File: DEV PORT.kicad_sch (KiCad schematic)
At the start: 11 parts

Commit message: added more notes and documentation
todo:
    - timing analysis to make sure everything fits in 250nS + hold time/prep time
    - logic analysis to ensure correct functionality (am gonna make dumb mistakes!)
    - board layout
    - physical testing!
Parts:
- added D?: (no value), symbol Diode:BAT48JFILM
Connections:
- net +5V: now also U?.48 (VIN), D?.1 (K)
- net at U?.49 (VUSB): now also D?.2 (A)
- no-connect marks 14 -> 13
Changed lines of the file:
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@@
   (no_connect (at 38.1 88.9))
   (no_connect (at 38.1 91.44))
-  (no_connect (at 93.98 21.59))
   (no_connect (at 69.85 113.03))
   (no_connect (at 73.66 113.03))
@@
     (pin "1")
   )
+  (symbol (lib_id "Diode:BAT48JFILM") (at 97.79 21.59 180) (unit 1)
+    (in_bom yes) (on_board yes) (fields_autoplaced)
+    (property "Reference" "D?" (id 0) (at 98.1075 15.24 0))
+    (property "Value" "" (id 1) (at 98.1075 17.78 0))
+    (property "Footprint" "" (id 2) (at 97.79 17.145 0)
+      (effects (font (size 1.27 1.27)) hide)
+    )
+    (property "Datasheet" "www.st.com/resource/en/datasheet/bat48.pdf" (id 3) (at 97.79 21.59 0)
+      (effects (font (size 1.27 1.27)) hide)
+    )
+    (pin "1")
+    (pin "2")
+  )
   (symbol (lib_id "power:+3V3") (at 153.67 81.28 0) (unit 1)
     (in_bom yes) (on_board yes) (fields_autoplaced)
@@
     )
     (property "Datasheet" "" (id 3) (at 251.46 110.49 0)
+      (effects (font (size 1.27 1.27)) hide)
+    )
+    (pin "1")
+  )
+  (symbol (lib_id "power:+5V") (at 93.98 25.4 270) (unit 1)
+    (in_bom yes) (on_board yes) (fields_autoplaced)
+    (property "Reference" "#PWR?" (id 0) (at 90.17 25.4 0)
+      (effects (font (size 1.27 1.27)) hide)
+    )
+    (property "Value" "" (id 1) (at 97.79 25.3999 90)
+      (effects (font (size 1.27 1.27)) (justify left))
+    )
+    (property "Footprint" "" (id 2) (at 93.98 25.4 0)
+      (effects (font (size 1.27 1.27)) hide)
+    )
+    (property "Datasheet" "" (id 3) (at 93.98 25.4 0)
       (effects (font (size 1.27 1.27)) hide)
     )
@@
     (pin "9")
   )
+  (symbol (lib_id "power:+5V") (at 101.6 21.59 270) (unit 1)
+    (in_bom yes) (on_board yes) (fields_autoplaced)
+    (property "Reference" "#PWR?" (id 0) (at 97.79 21.59 0)
+      (effects (font (size 1.27 1.27)) hide)
+    )
+    (property "Value" "" (id 1) (at 105.41 21.5899 90)
+      (effects (font (size 1.27 1.27)) (justify left))
+    )
+    (property "Footprint" "" (id 2) (at 101.6 21.59 0)
+      (effects (font (size 1.27 1.27)) hide)
+    )
+    (property "Datasheet" "" (id 3) (at 101.6 21.59 0)
+      (effects (font (size 1.27 1.27)) hide)
+    )
+    (pin "1")
+  )
   (symbol (lib_id "power:+3V3") (at 215.9 128.27 0) (unit 1)

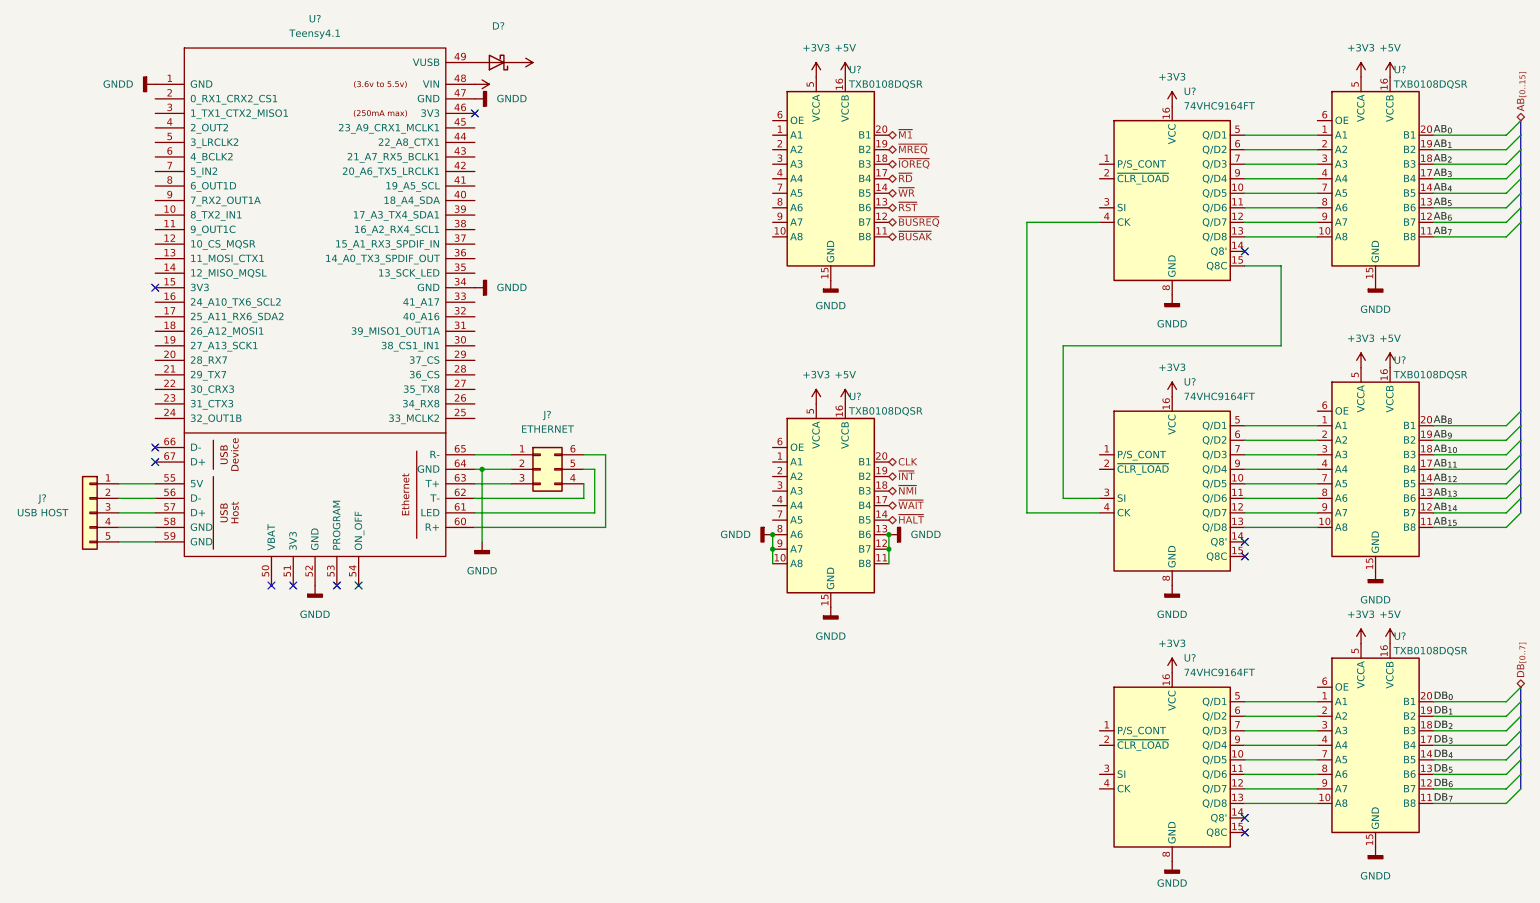
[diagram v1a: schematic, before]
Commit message: some clean up and simplification, as well as some renaming
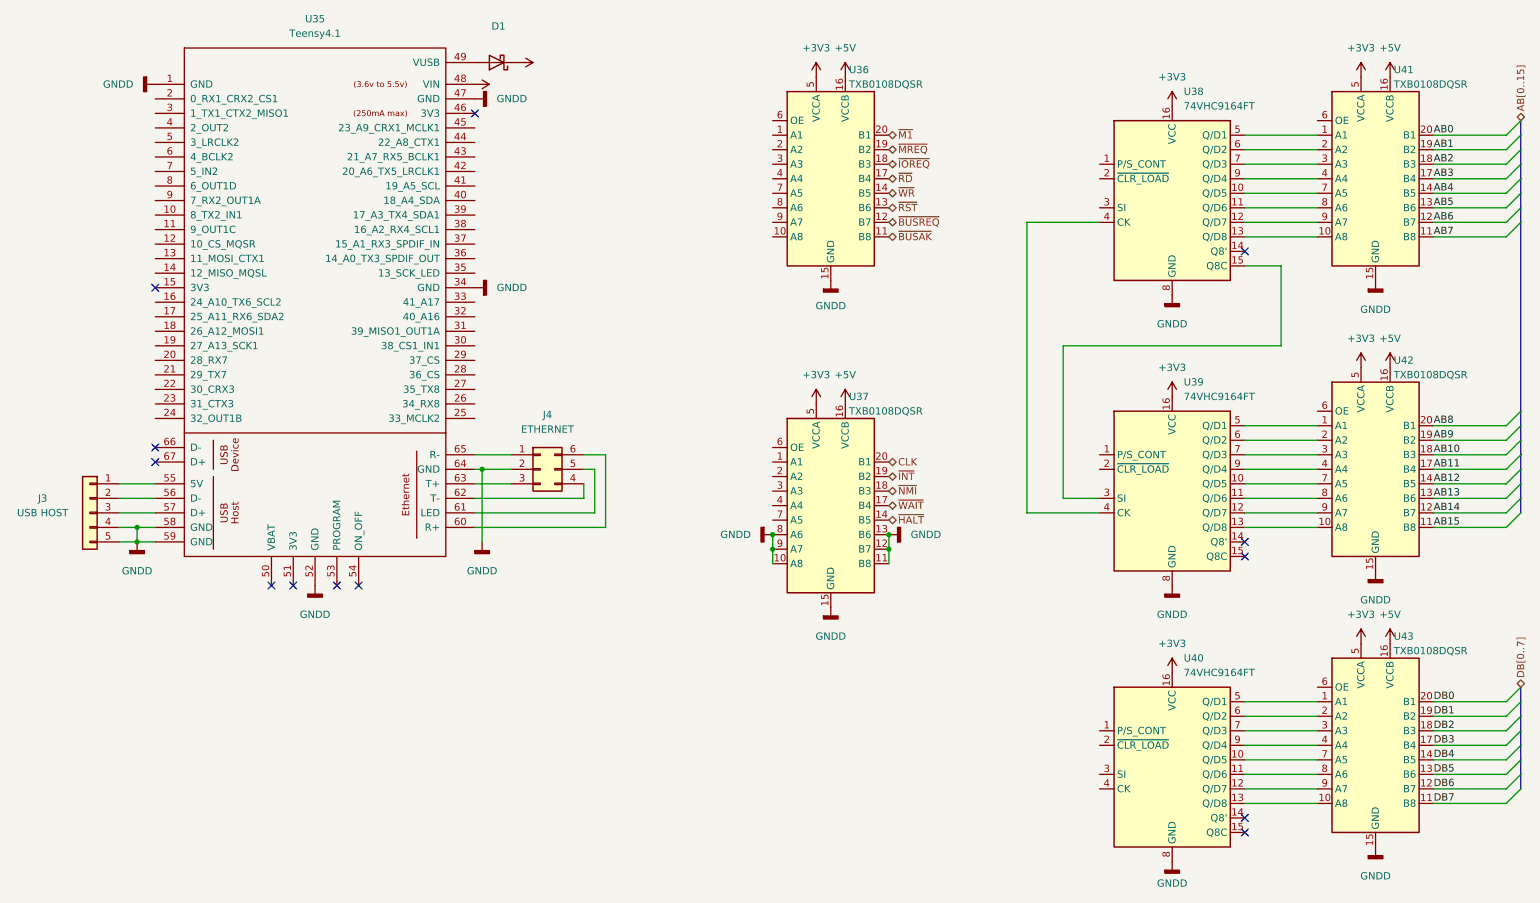
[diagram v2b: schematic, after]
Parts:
- gave numbers to parts that had none: 12
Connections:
- net GNDD: now also J3.4 (Pin_4), J3.5 (Pin_5), U35.58 (GND), U35.59 (GND)
- net AB_{0} renamed AB0
- net AB_{10} renamed AB10
- net AB_{11} renamed AB11
- net AB_{12} renamed AB12
- net AB_{13} renamed AB13
- net AB_{14} renamed AB14
- net AB_{15} renamed AB15
- net AB_{1} renamed AB1
- net AB_{2} renamed AB2
- net AB_{3} renamed AB3
- net AB_{4} renamed AB4
- net AB_{5} renamed AB5
- net AB_{6} renamed AB6
- net AB_{7} renamed AB7
- net AB_{8} renamed AB8
- net AB_{9} renamed AB9
- net DB_{0} renamed DB0
- net DB_{1} renamed DB1
- net DB_{2} renamed DB2
- net DB_{3} renamed DB3
- net DB_{4} renamed DB4
- net DB_{5} renamed DB5
- net DB_{6} renamed DB6
- net DB_{7} renamed DB7

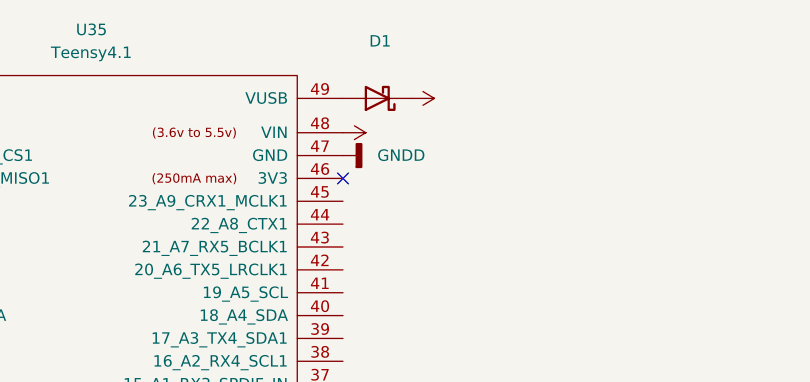
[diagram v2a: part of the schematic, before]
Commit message: begin integration of logic into atf1508
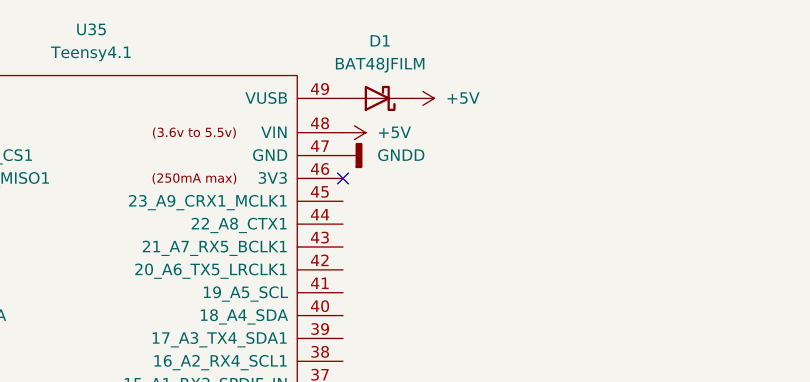
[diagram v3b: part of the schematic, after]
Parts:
- D1: value (none) -> BAT48JFILM; footprint (none) -> Diode_SMD:D_SOD-323
- J3: footprint (none) -> Connector_PinHeader_2.54mm:PinHeader_1x05_P2.54mm_Vertical
- J4: footprint (none) -> Connector_PinHeader_2.00mm:PinHeader_2x03_P2.00mm_Vertical
- U35: footprint (none) -> teensy:Teensy41
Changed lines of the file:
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@@
     (in_bom yes) (on_board yes) (fields_autoplaced)
     (property "Reference" "D1" (id 0) (at 98.1075 15.24 0))
-    (property "Value" "" (id 1) (at 98.1075 17.78 0))
-    (property "Footprint" "" (id 2) (at 97.79 17.145 0)
+    (property "Value" "BAT48JFILM" (id 1) (at 98.1075 17.78 0))
+    (property "Footprint" "Diode_SMD:D_SOD-323" (id 2) (at 97.79 17.145 0)
       (effects (font (size 1.27 1.27)) hide)
     )
@@
       (effects (font (size 1.27 1.27)) hide)
     )
-    (property "Value" "" (id 1) (at 97.79 25.3999 90)
+    (property "Value" "+5V" (id 1) (at 97.79 25.3999 90)
       (effects (font (size 1.27 1.27)) (justify left))
     )
@@
       (effects (font (size 1.27 1.27)) hide)
     )
-    (property "Value" "" (id 1) (at 105.41 21.5899 90)
+    (property "Value" "+5V" (id 1) (at 105.41 21.5899 90)
       (effects (font (size 1.27 1.27)) (justify left))
     )
@@
     (property "Reference" "J3" (id 0) (at 18.415 97.79 0))
     (property "Value" "USB HOST" (id 1) (at 18.415 100.33 0))
-    (property "Footprint" "" (id 2) (at 26.67 100.33 0)
+    (property "Footprint" "Connector_PinHeader_2.54mm:PinHeader_1x05_P2.54mm_Vertical" (id 2) (at 26.67 100.33 0)
       (effects (font (size 1.27 1.27)) hide)
     )
@@
     (property "Reference" "U35" (id 0) (at 66.04 13.97 0))
     (property "Value" "Teensy4.1" (id 1) (at 66.04 16.51 0))
-    (property "Footprint" "" (id 2) (at 55.88 69.85 0)
+    (property "Footprint" "teensy:Teensy41" (id 2) (at 55.88 69.85 0)
       (effects (font (size 1.27 1.27)) hide)
     )
@@
     (property "Reference" "J4" (id 0) (at 106.68 83.185 0))
     (property "Value" "ETHERNET" (id 1) (at 106.68 85.725 0))
-    (property "Footprint" "" (id 2) (at 105.41 92.71 0)
-      (effects (font (size 1.27 1.27)) hide)
-    )
+    (property "Footprint" "Connector_PinHeader_2.00mm:PinHeader_2x03_P2.00mm_Vertical" (id 2) (at 105.41 92.71 0)
+      (effects (font (size 1.27 1.27)) hide)
+    )
